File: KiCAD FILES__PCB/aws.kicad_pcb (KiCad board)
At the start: 2 copper layers, 214.9 x 91.5 mm, 33 parts, among them J17 B4B-XH-A_LF__SN_, J20 B3B-XH-A_LF__SN_, J21 B3B-XH-A_LF__SN_, J25 Screw_Terminal_01x02, J26 Screw_Terminal_01x02, J27 Screw_Terminal_01x02, J28 B4B-XH-A_LF__SN_, J3 B3B-XH-A_LF__SN_, J32 B3B-XH-A_LF__SN_, J37 B3B-XH-A_LF__SN_, J39 Conn_01x02_Pin, SW6 SW_SPST

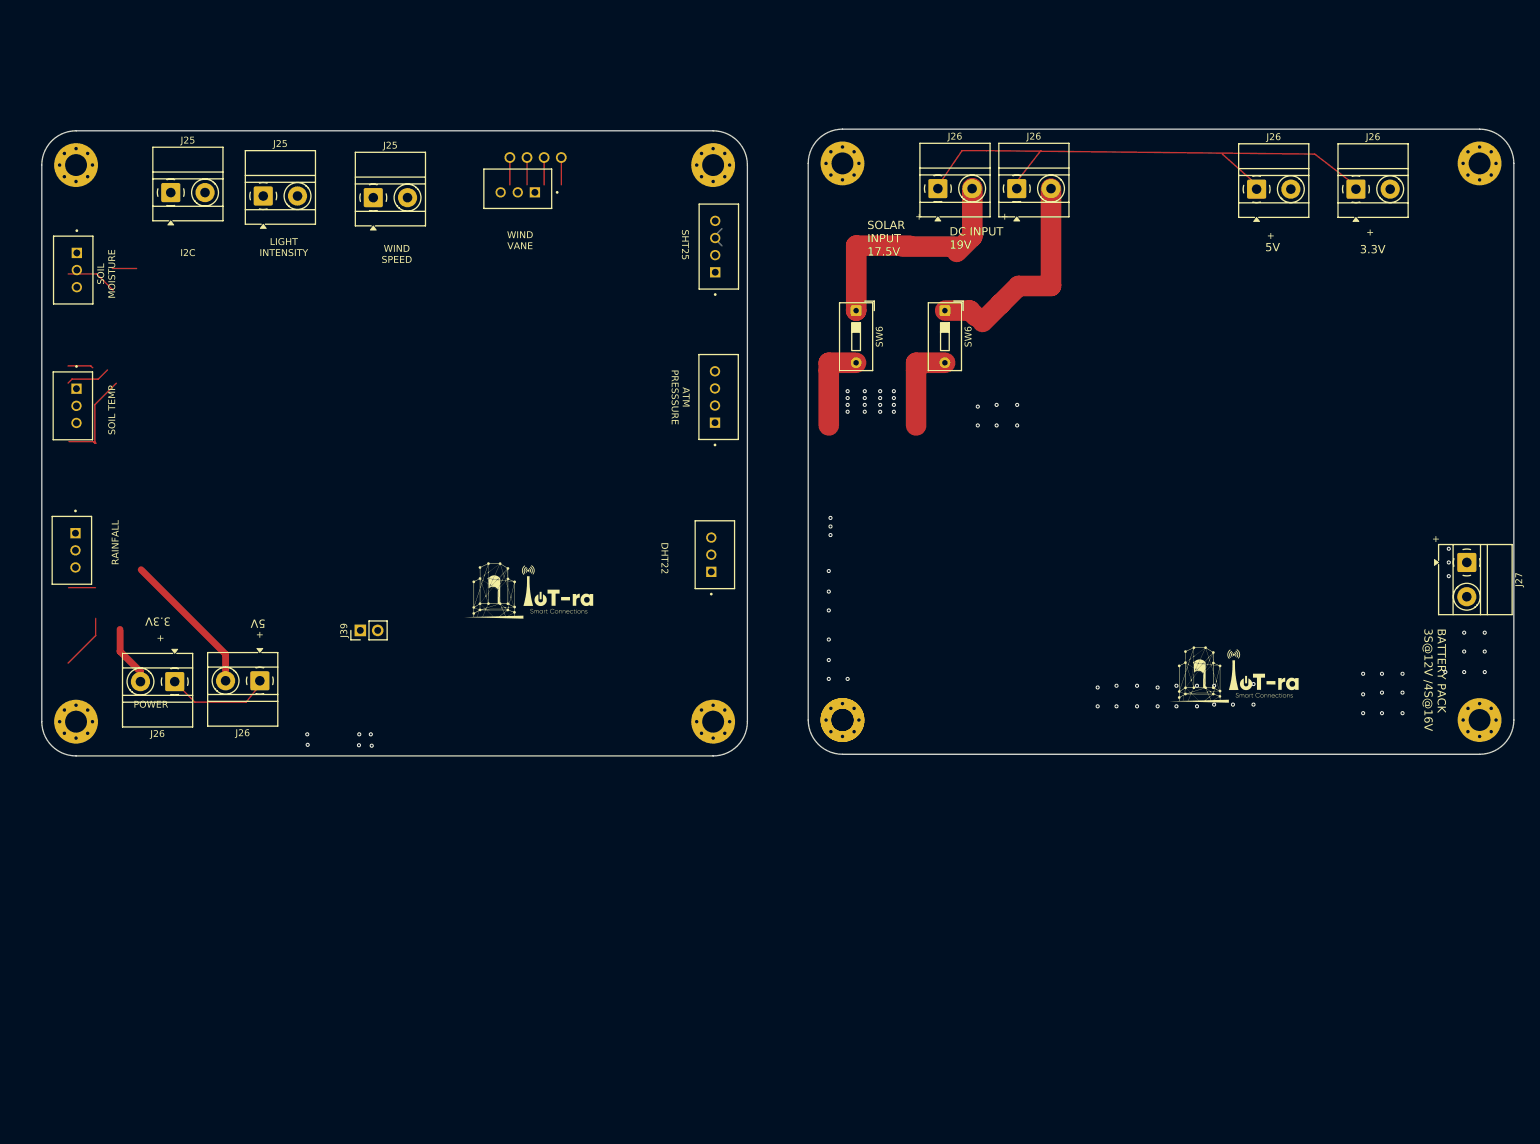
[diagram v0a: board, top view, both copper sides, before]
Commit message: Designed and routed the gateway board for the Automatic Weather Station
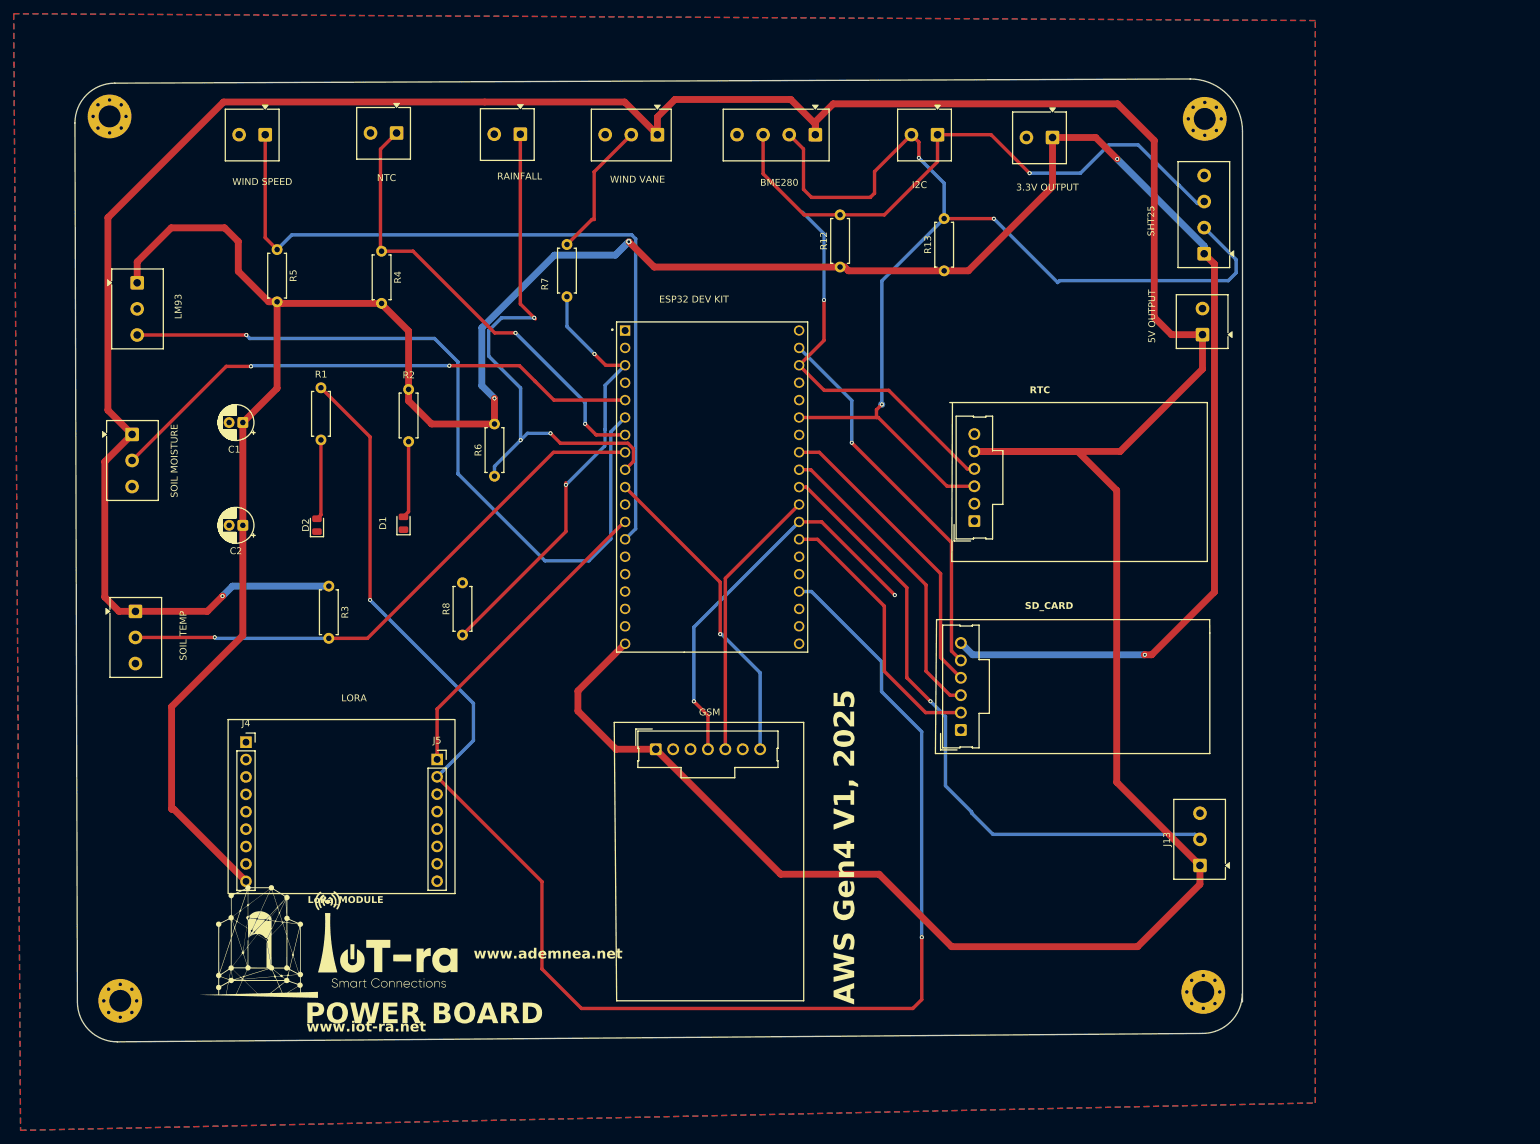
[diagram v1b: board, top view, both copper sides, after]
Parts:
- removed ? (x5): , 
- removed J20, J21, J32, J37: B3B-XH-A_LF__SN_, B3B-XH-A_LF__SN_:JST_B3B-XH-A_LF__SN_
- removed J25 (x3), J26 (x6), J27: Screw_Terminal_01x02, TerminalBlock_MetzConnect:TerminalBlock_MetzConnect_Type011_RT05502HBWC_1x02_P5.00mm_Horizontal
- removed J28: B4B-XH-A_LF__SN_, B4B-XH-A_LF__SN_:JST_B4B-XH-A_LF__SN_
- removed J39: Conn_01x02_Pin, Connector_PinHeader_2.54mm:PinHeader_1x02_P2.54mm_Vertical
- removed the REF** at (133.7, 123.3)
- removed the REF** at (133.7, 42.1)
- removed the REF** at (245.6, 123.1)
- removed the REF** at (40.7, 123.3)
- removed the REF** at (152.6, 123.1)
- removed the REF** at (245.6, 41.9)
- removed the REF** at (152.6, 41.9)
- removed the REF** at (40.7, 42.1)
- removed SW6 (x2): SW_SPST, Button_Switch_THT:SW_DIP_SPSTx01_Slide_9.78x4.72mm_W7.62mm_P2.54mm
- added C1: 10uF, Capacitor_THT:CP_Radial_D5.0mm_P2.00mm, F.Cu at (65.0, 79.7)
- added C2: 0.1uF, Capacitor_THT:CP_Radial_D5.0mm_P2.00mm, F.Cu at (65.0, 94.7)
- added D1: LED, LED_SMD:LED_0805_2012Metric, F.Cu at (88.5, 94.4)
- added D2: LED, LED_SMD:LED_0805_2012Metric, F.Cu at (75.8, 94.7)
- added J1: Real Time Clock, Connector_Molex:Molex_SL_171971-0006_1x06_P2.54mm_Vertical, F.Cu at (171.8, 94.1)
- added J10: WIND VANE, TerminalBlock_Phoenix:TerminalBlock_Phoenix_MKDS-1-3-3.81_1x03_P3.81mm_Horizontal, F.Cu at (125.5, 37.7)
- added J11: SD CARD, Connector_Molex:Molex_SL_171971-0006_1x06_P2.54mm_Vertical, F.Cu at (169.8, 124.6)
- added J11: SOIL MOISTURE, TerminalBlock_Phoenix:TerminalBlock_Phoenix_MKDS-1-3-3.81_1x03_P3.81mm_Horizontal, F.Cu at (48.9, 81.4)
- added J12: SOIL TEMP, TerminalBlock_Phoenix:TerminalBlock_Phoenix_MKDS-1-3-3.81_1x03_P3.81mm_Horizontal, F.Cu at (49.3, 107.2)
- added J13: DHT 22, TerminalBlock_Phoenix:TerminalBlock_Phoenix_MKDS-1-3-3.81_1x03_P3.81mm_Horizontal, F.Cu at (204.7, 144.3)
- added J14: SHT25, TerminalBlock_Phoenix:TerminalBlock_Phoenix_MKDS-1-4-3.81_1x04_P3.81mm_Horizontal, F.Cu at (205.3, 55.0)
- added J15: NTC THERMISTOR, TerminalBlock_Phoenix:TerminalBlock_Phoenix_MKDS-1-2-3.81_1x02_P3.81mm_Horizontal, F.Cu at (87.5, 37.4)
- added J18: 3.3V, TerminalBlock_Phoenix:TerminalBlock_Phoenix_MKDS-1-2-3.81_1x02_P3.81mm_Horizontal, F.Cu at (183.2, 38.1)
- added J2: GSM, Connector_Molex:Molex_SL_171971-0007_1x07_P2.54mm_Vertical, F.Cu at (125.3, 127.4)
- added J4: Conn_01x09_Socket, Connector_PinSocket_2.54mm:PinSocket_1x09_P2.54mm_Vertical, F.Cu at (65.5, 126.3)
- added J5: Conn_01x08_Socket, Connector_PinSocket_2.54mm:PinSocket_1x08_P2.54mm_Vertical, F.Cu at (93.4, 128.9)
- added J6: I2C, TerminalBlock_Phoenix:TerminalBlock_Phoenix_MKDS-1-2-3.81_1x02_P3.81mm_Horizontal, F.Cu at (166.4, 37.7)
- added J7: WIND SPEED, TerminalBlock_Phoenix:TerminalBlock_Phoenix_MKDS-1-2-3.81_1x02_P3.81mm_Horizontal, F.Cu at (68.3, 37.7)
- added J8: LM93, TerminalBlock_Phoenix:TerminalBlock_Phoenix_MKDS-1-3-3.81_1x03_P3.81mm_Horizontal, F.Cu at (49.6, 59.3)
- added J9: RAINFALL SENSOR, TerminalBlock_Phoenix:TerminalBlock_Phoenix_MKDS-1-2-3.81_1x02_P3.81mm_Horizontal, F.Cu at (105.5, 37.6)
- added R1: 1k, Resistor_THT:R_Axial_DIN0207_L6.3mm_D2.5mm_P7.62mm_Horizontal, F.Cu at (76.4, 74.6)
- added R12: 4.7k, Resistor_THT:R_Axial_DIN0207_L6.3mm_D2.5mm_P7.62mm_Horizontal, F.Cu at (152.2, 57.0)
- added R13: 4.7k, Resistor_THT:R_Axial_DIN0207_L6.3mm_D2.5mm_P7.62mm_Horizontal, F.Cu at (167.4, 57.5)
- added R2: 0.47k, Resistor_THT:R_Axial_DIN0207_L6.3mm_D2.5mm_P7.62mm_Horizontal, F.Cu at (89.2, 74.8)
- added R3: 4.7k, Resistor_THT:R_Axial_DIN0207_L6.3mm_D2.5mm_P7.62mm_Horizontal, F.Cu at (77.6, 103.6)
- added R4: 4.7k, Resistor_THT:R_Axial_DIN0207_L6.3mm_D2.5mm_P7.62mm_Horizontal, F.Cu at (85.3, 54.7)
- added R5: 4.7k, Resistor_THT:R_Axial_DIN0207_L6.3mm_D2.5mm_P7.62mm_Horizontal, F.Cu at (70.0, 54.4)
- added R6: 4.7k, Resistor_THT:R_Axial_DIN0207_L6.3mm_D2.5mm_P7.62mm_Horizontal, F.Cu at (101.8, 87.5)
- added R7: 1k, Resistor_THT:R_Axial_DIN0207_L6.3mm_D2.5mm_P7.62mm_Horizontal, F.Cu at (112.3, 53.7)
- added R8: 2k, Resistor_THT:R_Axial_DIN0207_L6.3mm_D2.5mm_P7.62mm_Horizontal, F.Cu at (97.1, 110.7)
- added REF**: MountingHole_3.2mm_M3_Pad_Via, MountingHole:MountingHole_3.2mm_M3_Pad_Via, F.Cu at (47.1, 164.1)
- added REF**: MountingHole_3.2mm_M3_Pad_Via, MountingHole:MountingHole_3.2mm_M3_Pad_Via, F.Cu at (205.2, 162.8)
- added REF**: MountingHole_3.2mm_M3_Pad_Via, MountingHole:MountingHole_3.2mm_M3_Pad_Via, F.Cu at (45.6, 35.0)
- added REF**: MountingHole_3.2mm_M3_Pad_Via, MountingHole:MountingHole_3.2mm_M3_Pad_Via, F.Cu at (205.4, 35.4)
- added U1: ESP32-DEVKITC-32U, esp32devkit:MODULE_ESP32-DEVKITC-32U, F.Cu at (133.5, 89.1)
- J17: value B4B-XH-A_LF__SN_ -> BME280; footprint B4B-XH-A_LF__SN_:JST_B4B-XH-A_LF__SN_ -> TerminalBlock_Phoenix:TerminalBlock_Phoenix_MKDS-1-4-3.81_1x04_P3.81mm_Horizontal
- J3: value B3B-XH-A_LF__SN_ -> 5V; footprint B3B-XH-A_LF__SN_:JST_B3B-XH-A_LF__SN_ -> TerminalBlock_Phoenix:TerminalBlock_Phoenix_MKDS-1-2-3.81_1x02_P3.81mm_Horizontal
- moved J3 168.0 mm to (205.1, 66.9)
- moved J17 21.6 mm to (148.6, 37.7), turned to 180 degrees
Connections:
- J17 pad 1: +3.3V_LORA -> +5V
- J17 pad 2: /gate way/I2C SCL -> G21
- J17 pad 3: /gate way/I2C SDA -> G22
- J3 pad 1: /gate way/DAVIS 7852 -> +5V
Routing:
- net +5V: track 0.00 -> 550.8 mm, vias 0 -> 1
- net +3.3V: track 0.00 -> 412.2 mm, vias 0 -> 4
- net G15: track 0.00 -> 229.1 mm, vias 0 -> 2
- net G21: track 0.00 -> 163.4 mm, vias 0 -> 3
- net G22: track 0.00 -> 144.6 mm, vias 0 -> 2
- net G12: track 0.00 -> 115.5 mm
- net G35: track 0.00 -> 112.4 mm, vias 0 -> 1
- net G5: track 0.00 -> 93.5 mm, vias 0 -> 1
- net G33: track 0.00 -> 82.8 mm, vias 0 -> 1
- net G25: track 0.00 -> 81.4 mm, vias 0 -> 3
- net G34: track 0.00 -> 80.2 mm, vias 0 -> 2
- net G32: track 0.00 -> 66.9 mm, vias 0 -> 2
- net Net-(J26-Pin_2): track 66.7 -> 0.00 mm
- net G36: track 0.00 -> 64.8 mm, vias 0 -> 2
- net G16: track 0.00 -> 58.8 mm, vias 0 -> 2
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- added copper zone on B.Cu, net GND
- added copper zone on F.Cu, net GND
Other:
- board size 214.9 x 91.5 mm -> 170.4 x 140.6 mm
- board text added: "3.3V OUTPUT"
- board text added: "5V OUTPUT"
- board text added: "BME280"
- board text added: "ESP32 DEV KIT"
- board text added: "GSM"
- board text added: "LM93"
- board text added: "LORA"
- board text added: "LoRa_MODULE"
- board text added: "NTC"
- board text added: "RTC"
- board text added: "SD_CARD"
- board text removed: "+"
- board text removed: "3.3V"
- board text removed: "3V"
- board text removed: "5V"
- board text removed: "ATM PRESSSURE"
- board text removed: "BATTERY PACK 3S@12V /4S@16V"
- board text removed: "DC INPUT 19V"
- board text removed: "DHT22"
- board text removed: "G"
- board text removed: "GATE WAY BOARD"
- board text removed: "LIGHT INTENSITY"
- board text removed: "POWER"
- board text removed: "SOLAR INPUT 17.5V"
